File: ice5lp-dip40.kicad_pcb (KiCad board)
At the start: 2 copper layers, 17.8 x 50.8 mm, 48 parts, among them J1 Conn_02x04_Odd_Even, J2 Conn_01x20, J3 Conn_01x20, J4 USB_B_Micro, SW1 SW_Push, SW2 SW_Push, U1 AT25D011-SSHF, U2 MIC5355-S4YMME, U3 ICE5LP4K-SG48, X1 ECS-2520MV-500-BN-TR

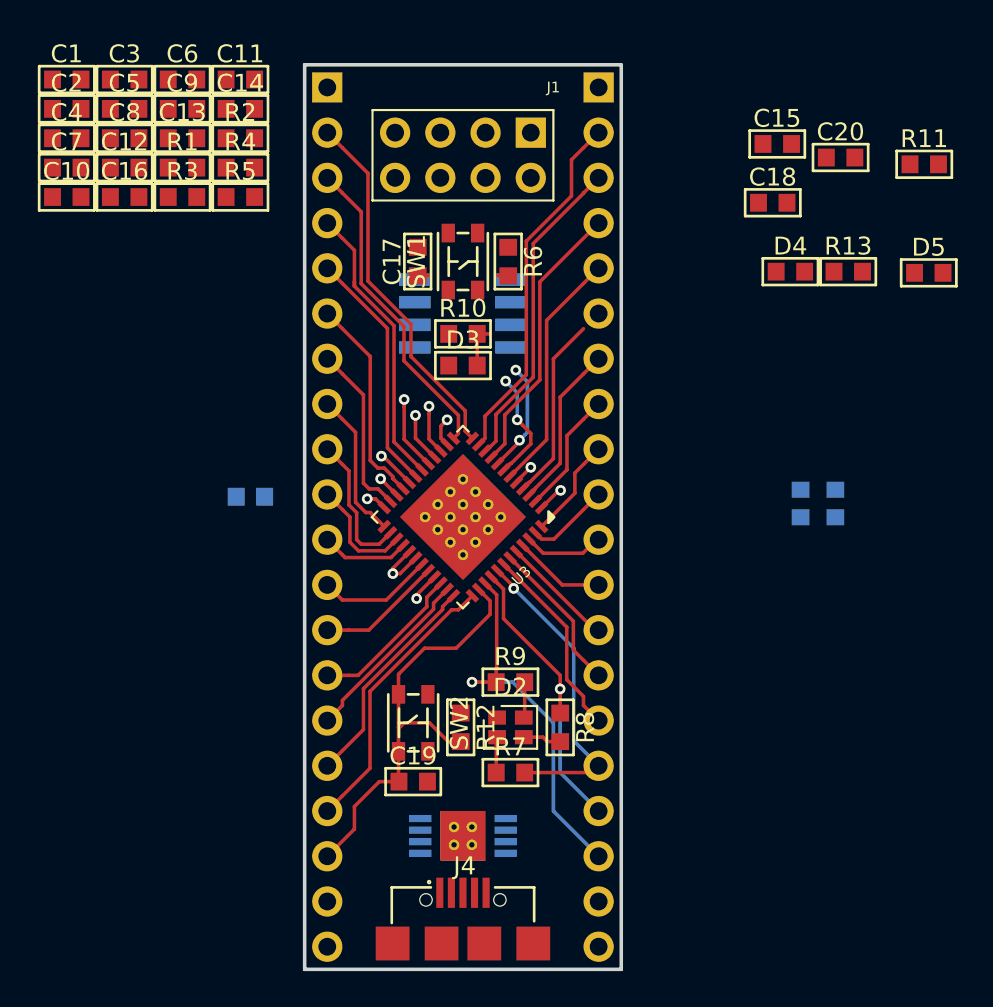
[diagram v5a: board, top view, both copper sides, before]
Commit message: Place and trace all main components
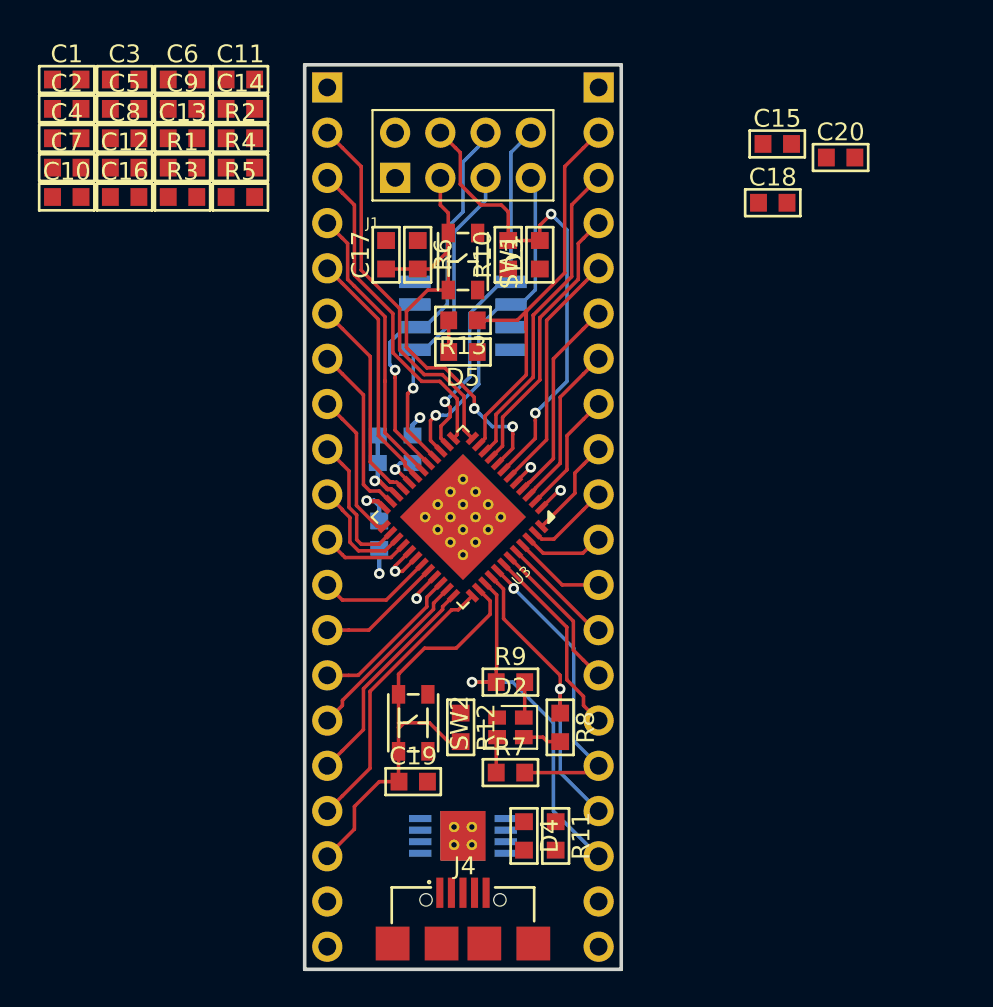
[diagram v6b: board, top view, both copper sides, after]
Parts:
- moved R11 43.0 mm to (200.8, 100.5), turned to 270 degrees
- moved D4 35.0 mm to (199.0, 100.5), turned to 270 degrees
- moved D5 26.5 mm to (195.6, 73.3), turned to 180 degrees
- moved X1 23.9 mm to (191.8, 78.7)
- moved R13 21.8 mm to (195.6, 71.5), turned to 180 degrees
- moved J1 8.03 mm to (191.8, 63.5), turned to 90 degrees
- moved D3 7.57 mm to (199.9, 67.8), turned to 90 degrees
- moved D1 7.55 mm to (190.9, 83.6), turned to 270 degrees
- moved R10 5.12 mm to (198.1, 67.8), turned to 90 degrees
- moved R6 5.09 mm to (193.0, 67.8)
- moved C17 1.82 mm to (191.3, 67.8)
- moved U1 0.13 mm to (195.6, 71.2)
- turned SW1 to 270 degrees
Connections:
- J1 pad 3: CDONE -> CRESET
- J1 pad 4: CRESET -> CDONE
- J1 pad 5: FLASH_MISO -> ICE_CSN
- J1 pad 6: ICE_SCK -> FLASH_MISO
- J1 pad 7: ICE_CSN -> ICE_SCK
- J3 pad 2: IOB_20A -> ICE_LED
- R13 pad 1: (no net) -> ICE_LED
- U3 pad 11: IOB_20A -> ICE_LED
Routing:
- net ICE_LED: track 0.00 -> 24.3 mm
- net IOB_20A: track 20.3 -> 0.00 mm
- net CRESET: track 7.61 -> 27.5 mm
- net CDONE: track 8.68 -> 28.0 mm
- net FLASH_MOSI: track 1.69 -> 20.3 mm
- net FLASH_MISO: track 4.16 -> 22.3 mm
- net ICE_SCK: track 2.79 -> 19.2 mm
- net ICE_CSN: track 2.80 -> 18.5 mm
- net VCC_IO0: track 4.40 -> 8.66 mm, vias 3 -> 4
- net Net-(D5-Pad2): track 0.00 -> 1.78 mm
- net Net-(D1-Pad1): track 1.16 -> 2.89 mm
- net IOB_8A: track 10.4 -> 11.6 mm
- net GND: track 0.00 -> 1.18 mm, vias 0 -> 1
- net IOB_22A: track 20.5 -> 21.1 mm
- net IOB_24A: track 17.8 -> 18.3 mm
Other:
- net class Power added: clearance 0.2, trace_width 0.3, via_dia 0.7, via_drill 0.4

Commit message: Place some caps
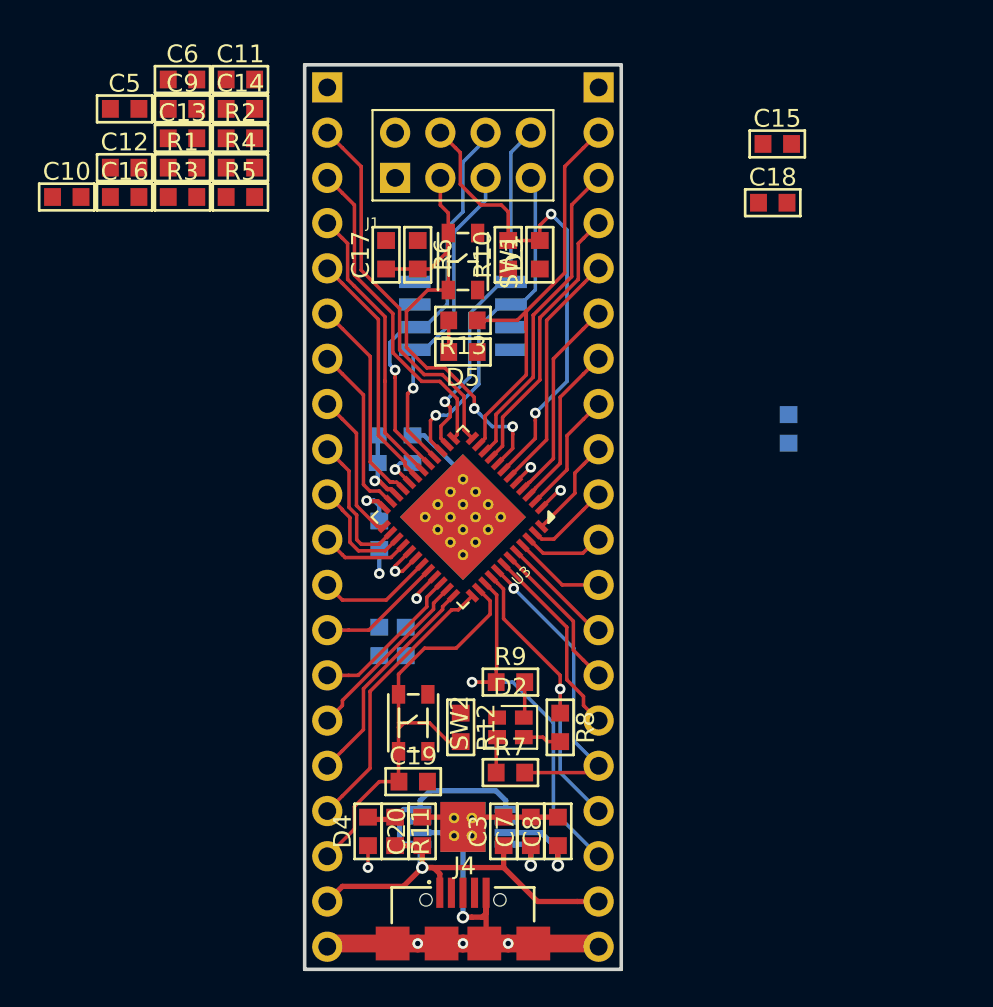
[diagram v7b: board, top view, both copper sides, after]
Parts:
- C1, C2, C4: moved to B.Cu
- moved C3 47.3 mm to (197.9, 100.2), turned to 90 degrees
- moved C8 45.9 mm to (200.9, 100.2), turned to 90 degrees
- moved C7 45.5 mm to (199.4, 100.2), turned to 90 degrees
- moved C1 45.0 mm to (213.9, 77.6), turned to 90 degrees
- moved C20 44.5 mm to (193.3, 100.2), turned to 90 degrees
- moved C2 35.5 mm to (192.4, 89.5), turned to 270 degrees
- moved C4 33.3 mm to (190.9, 89.5), turned to 270 degrees
- moved R11 9.02 mm to (191.8, 100.2)
- moved D4 8.77 mm to (190.2, 100.2), turned to 90 degrees
- moved U2 0.51 mm to (195.6, 99.9)
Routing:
- net GND: track 1.18 -> 43.1 mm, vias 1 -> 5
- net +5V: track 0.00 -> 34.5 mm, vias 0 -> 1
- net VCC_CORE: track 4.09 -> 9.41 mm, vias 2 -> 3
- net VCC_IO0: track 8.66 -> 12.1 mm, vias 4 -> 5
- net Net-(D4-Pad2): track 0.00 -> 1.52 mm

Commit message: Beautify schematic and place all components on PCB
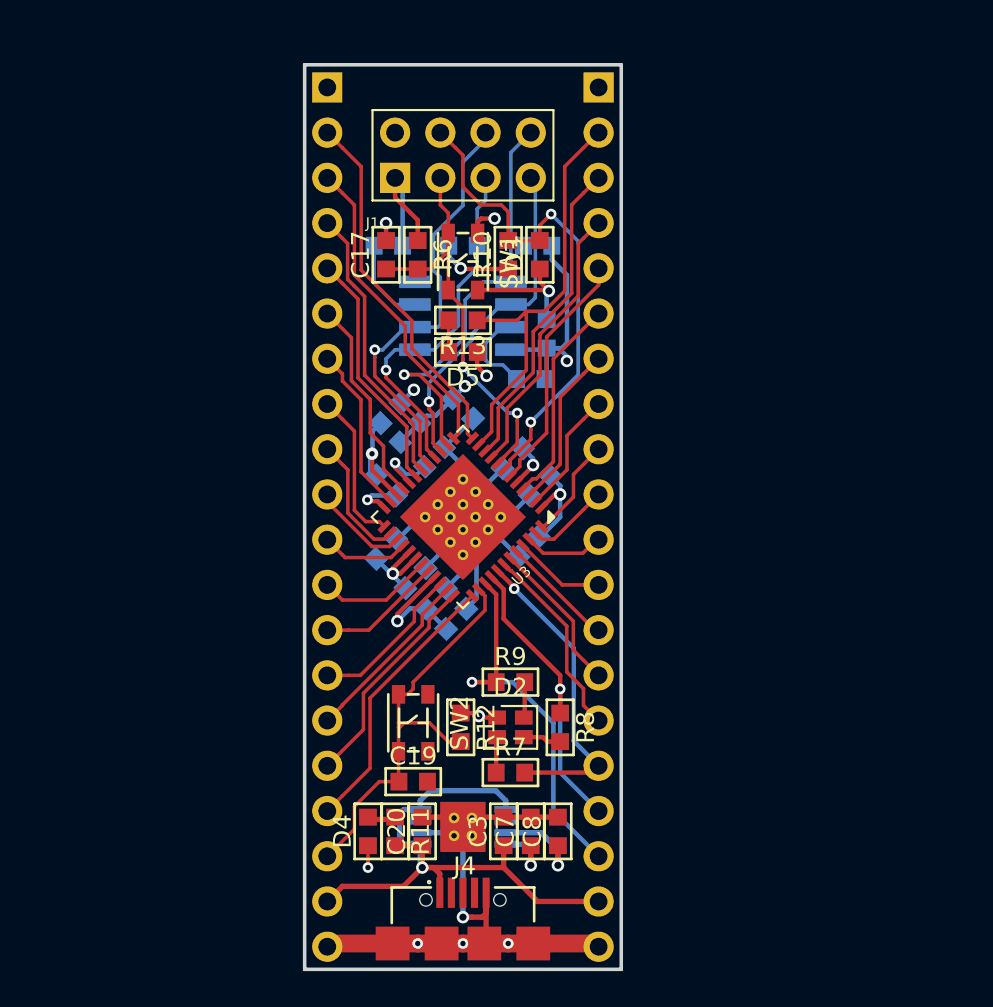
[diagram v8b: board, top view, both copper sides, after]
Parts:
- removed C14, C5: 1u, esynr3z_Capacitor:C_0603
- removed C16, C6: 100n, esynr3z_Capacitor:C_0603
- removed R3: 100, esynr3z_Resistor:R_0603
- C10, C11, C13, C15, C18, C9, R1, R2, R4, R5: moved to B.Cu
- C12: value 1u -> 100n; moved to B.Cu
- moved C11 32.6 mm to (195.2, 88.3), turned to 45 degrees
- moved C12 31.1 mm to (199.3, 84.2), turned to 225 degrees
- moved C13 29.5 mm to (194.1, 87.1), turned to 45 degrees
- moved C9 29.2 mm to (199.9, 80.8), turned to 225 degrees
- moved C10 28.0 mm to (200.3, 72.3), turned to 90 degrees
- moved C15 26.5 mm to (191.5, 76.7), turned to 45 degrees
- moved C1 22.6 mm to (192.9, 86.0), turned to 45 degrees
- moved C18 20.9 mm to (195.6, 76.5), turned to 315 degrees
- moved R4 20.2 mm to (199.4, 74.8), turned to 180 degrees
- moved R5 16.9 mm to (199.8, 67.3), turned to 180 degrees
- moved R1 16.3 mm to (195.6, 67.3)
- moved C2 11.9 mm to (198.4, 79.2), turned to 225 degrees
- moved R2 10.3 mm to (191.4, 67.3), turned to 180 degrees
- moved C4 5.22 mm to (191.3, 84.3), turned to 45 degrees
- moved D1 2.82 mm to (191.3, 80.8), turned to 135 degrees
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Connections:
- net VCC_IO0 renamed VCC_IO
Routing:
- net VCC_IO: track 12.1 -> 53.9 mm, vias 5 -> 8
- net GND: track 43.1 -> 83.7 mm, vias 5 -> 10
- net Net-(R4-Pad2): track 0.00 -> 4.96 mm
- net Net-(R2-Pad2): track 0.00 -> 4.89 mm
- net VCC_CORE: track 9.41 -> 13.5 mm
- net CRESET: track 27.5 -> 24.1 mm
- net FLASH_MOSI: track 20.3 -> 23.7 mm
- net ICE_CSN: track 18.5 -> 20.4 mm
- net FLASH_MISO: track 22.3 -> 24.1 mm
- net ICE_CLK: track 2.29 -> 3.54 mm
- net ICE_BTN: track 24.8 -> 23.8 mm
- net IOT_39A: track 8.04 -> 7.21 mm
- net IOT_38B: track 6.32 -> 5.53 mm
- net ICE_SCK: track 19.2 -> 19.8 mm
- net IOB_22A: track 21.1 -> 20.5 mm
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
